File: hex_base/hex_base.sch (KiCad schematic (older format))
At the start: 41 parts, among them J1 ESP_proc, J10 PANEL5, J2 E75_proc, J3 USB_C, J4 PANEL0, J5 PANEL0, J6 PANEL1, J7 PANEL2, J8 PANEL3, J9 PANEL4, P1 TC2030-ESP, P2 TC2030-E75, U1 ESP32-WROOM-32, U2 E75-2G4M20S, U3 AMS1117-3.3

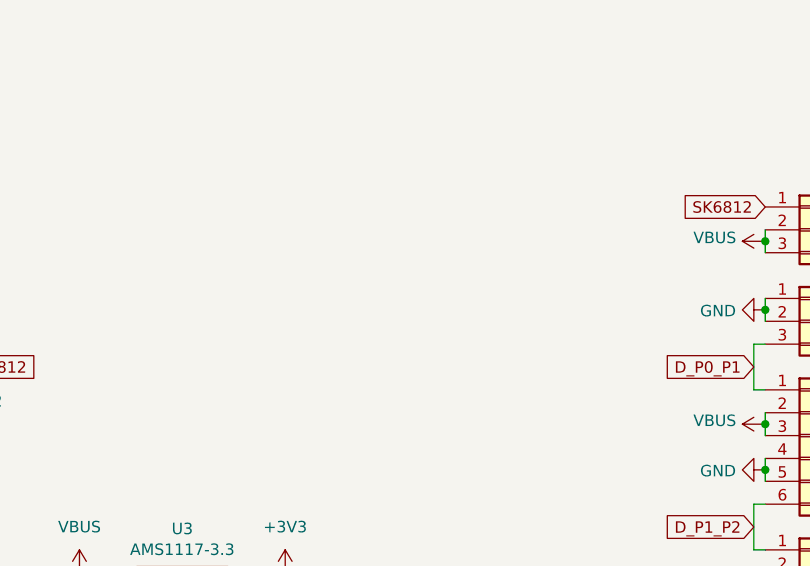
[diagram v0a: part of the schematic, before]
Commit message: fitted led board onto base, todo: buttons, fix light sensor, more caps?, silkscreen
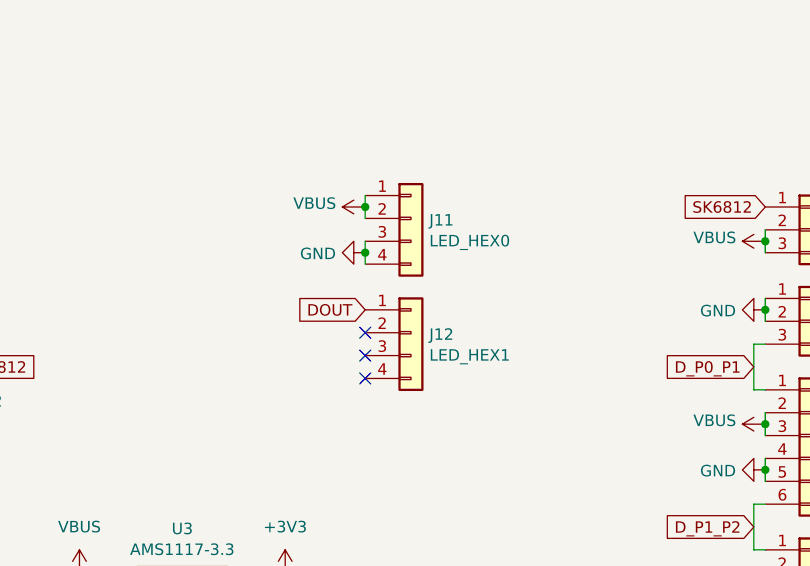
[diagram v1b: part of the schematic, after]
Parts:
- added J11: LED_HEX0, otter:PinSocket_1x04_P2.54mm_Vertical_center, symbol Connector_Generic:Conn_01x04
- added J12: LED_HEX1, otter:PinSocket_1x04_P2.54mm_Vertical_center, symbol Connector_Generic:Conn_01x04
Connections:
- net DOUT: now also J12.1 (Pin_1)
- net GND: now also J11.3 (Pin_3), J11.4 (Pin_4)
- net VBUS: now also J11.1 (Pin_1), J11.2 (Pin_2)
- no-connect marks 41 -> 44
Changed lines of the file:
@@
 Wire Wire Line
 	8300 1900 8300 1950
-Text GLabel 8300 5550 0    50   Input ~ 0
-DOUT
 Wire Wire Line
 	1800 6950 1800 7600
@@
 Wire Wire Line
 	1800 6950 2000 6950
+$Comp
+L Connector_Generic:Conn_01x04 J11
+U 1 1 61E2192F
+P 6750 1500
+F 0 "J11" H 6830 1492 50  0000 L CNN
+F 1 "LED_HEX0" H 6830 1401 50  0000 L CNN
+F 2 "otter:PinSocket_1x04_P2.54mm_Vertical_center" H 6750 1500 50  0001 C CNN
+F 3 "~" H 6750 1500 50  0001 C CNN
+	1    6750 1500
+	1    0    0    -1
+$EndComp
+Wire Wire Line
+	6550 1500 6550 1450
+Wire Wire Line
+	6550 1600 6550 1650
+Text GLabel 8300 5550 0    50   Input ~ 0
+DOUT
+Text GLabel 6550 1900 0    50   Input ~ 0
+DOUT
+$Comp
+L power:VBUS #PWR0151
+U 1 1 61E2EE7B
+P 6550 1450
+F 0 "#PWR0151" H 6550 1300 50  0001 C CNN
+F 1 "VBUS" V 6565 1577 50  0000 L CNN
+F 2 "" H 6550 1450 50  0001 C CNN
+F 3 "" H 6550 1450 50  0001 C CNN
+	1    6550 1450
+	0    -1   -1   0
+$EndComp
+$Comp
+L otter:GND #PWR0152
+U 1 1 61E2EE81
+P 6550 1650
+F 0 "#PWR0152" H 6550 1400 50  0001 C CNN
+F 1 "GND" V 6555 1522 50  0000 R CNN
+F 2 "" H 6550 1650 60  0000 C CNN
+F 3 "" H 6550 1650 60  0000 C CNN
+	1    6550 1650
+	0    1    1    0
+$EndComp
+Connection ~ 6550 1450
+Wire Wire Line
+	6550 1450 6550 1400
+Connection ~ 6550 1650
+Wire Wire Line
+	6550 1650 6550 1700
+NoConn ~ 6550 2000
+$Comp
+L Connector_Generic:Conn_01x04 J12
+U 1 1 61E22468
+P 6750 2000
+F 0 "J12" H 6830 1992 50  0000 L CNN
+F 1 "LED_HEX1" H 6830 1901 50  0000 L CNN
+F 2 "otter:PinSocket_1x04_P2.54mm_Vertical_center" H 6750 2000 50  0001 C CNN
+F 3 "~" H 6750 2000 50  0001 C CNN
+	1    6750 2000
+	1    0    0    -1
+$EndComp
+NoConn ~ 6550 2100
+NoConn ~ 6550 2200
 $EndSCHEMATC

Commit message: finished base, exported gerber
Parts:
- added C12: 100n, otter:C_0402, symbol Device:C_Small
- added R15: 100k, otter:R_0402, symbol Device:R_Small
- added SW1: RST, Button_Switch_SMD:SW_SPST_PTS810, symbol Switch:SW_Push
- added SW2: BIND, Button_Switch_SMD:SW_SPST_PTS810, symbol Switch:SW_Push
- R1: footprint otter:R_0402 -> otter:R_0805
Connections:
- net E75_RST: now also SW2.2
- net ESP_EN: now also SW1.2
- net GND: now also C12.2, SW1.1, SW2.1
- net PWM_1: now also R15.2
- net at U1.8 (IO32): now also C12.1, R15.1
- no-connect marks 44 -> 43
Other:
- moved on the sheet: J1
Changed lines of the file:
@@
 	1    0    0    -1
 $EndComp
-Text GLabel 1900 5950 0    50   Input ~ 0
+Text GLabel 1750 5850 1    50   Input ~ 0
 E75_RST
 NoConn ~ 2000 6150
@@
 $EndComp
 Wire Wire Line
-	1900 5950 1950 5950
-Wire Wire Line
 	1950 5850 1950 5950
 Connection ~ 1950 5950
@@
 NoConn ~ 3100 3250
 NoConn ~ 3100 3450
-NoConn ~ 3100 3950
 NoConn ~ 3100 3850
 NoConn ~ 3100 3750
@@
 	3100 4050 4000 4050
 $Comp
-L Device:R_Small R10
-U 1 1 61CCA13E
-P 4200 4050
-F 0 "R10" V 4500 4100 50  0000 C CNN
-F 1 "100k" V 4500 3900 50  0000 C CNN
-F 2 "otter:R_0402" H 4200 4050 50  0001 C CNN
-F 3 "~" H 4200 4050 50  0001 C CNN
-	1    4200 4050
-	0    -1   -1   0
-$EndComp
-$Comp
 L Device:R_Small R11
 U 1 1 61CCA8FD
 P 4200 4150
-F 0 "R11" V 4500 4200 50  0000 C CNN
-F 1 "100k" V 4500 4000 50  0000 C CNN
+F 0 "R11" V 4650 4200 50  0000 C CNN
+F 1 "100k" V 4650 4000 50  0000 C CNN
 F 2 "otter:R_0402" H 4200 4150 50  0001 C CNN
 F 3 "~" H 4200 4150 50  0001 C CNN
@@
 U 1 1 61CCAB94
 P 4200 4250
-F 0 "R12" V 4500 4300 50  0000 C CNN
-F 1 "100k" V 4500 4100 50  0000 C CNN
+F 0 "R12" V 4650 4300 50  0000 C CNN
+F 1 "100k" V 4650 4100 50  0000 C CNN
 F 2 "otter:R_0402" H 4200 4250 50  0001 C CNN
 F 3 "~" H 4200 4250 50  0001 C CNN
@@
 F 0 "R1" H 1020 2096 50  0000 L CNN
 F 1 "R_PHOTO" H 1020 2005 50  0000 L CNN
-F 2 "otter:R_0402" V 1000 1800 50  0001 L CNN
+F 2 "otter:R_0805" V 1000 1800 50  0001 L CNN
 F 3 "~" H 950 2000 50  0001 C CNN
 	1    950  2050
@@
 Wire Wire Line
 	1800 1850 1800 1950
-Wire Wire Line
-	1800 1950 1750 1950
 Connection ~ 1800 1950
-Text GLabel 1750 1950 0    50   Input ~ 0
+Text GLabel 1500 1600 1    50   Input ~ 0
 ESP_EN
 Text GLabel 3100 2050 2    50   Input ~ 0
@@
 L Connector_Generic:Conn_01x05 J1
 U 1 1 61CE5F79
-P 900 1100
-F 0 "J1" H 818 675 50  0000 C CNN
-F 1 "ESP_proc" H 818 766 50  0000 C CNN
-F 2 "Connector_PinHeader_2.54mm:PinHeader_1x05_P2.54mm_Vertical" H 900 1100 50  0001 C CNN
-F 3 "~" H 900 1100 50  0001 C CNN
-	1    900  1100
+P 850 4400
+F 0 "J1" H 768 3975 50  0000 C CNN
+F 1 "ESP_proc" H 768 4066 50  0000 C CNN
+F 2 "Connector_PinHeader_2.54mm:PinHeader_1x05_P2.54mm_Vertical" H 850 4400 50  0001 C CNN
+F 3 "~" H 850 4400 50  0001 C CNN
+	1    850  4400
 	-1   0    0    1
 $EndComp
@@
 L otter:GND #PWR0123
 U 1 1 61CE6E5C
-P 1100 1300
-F 0 "#PWR0123" H 1100 1050 50  0001 C CNN
-F 1 "GND" H 1105 1127 50  0000 C CNN
-F 2 "" H 1100 1300 60  0000 C CNN
-F 3 "" H 1100 1300 60  0000 C CNN
-	1    1100 1300
-	1    0    0    -1
-$EndComp
-Text GLabel 1100 1000 2    50   Input ~ 0
+P 1050 4600
+F 0 "#PWR0123" H 1050 4350 50  0001 C CNN
+F 1 "GND" H 1055 4427 50  0000 C CNN
+F 2 "" H 1050 4600 60  0000 C CNN
+F 3 "" H 1050 4600 60  0000 C CNN
+	1    1050 4600
+	1    0    0    -1
+$EndComp
+Text GLabel 1050 4300 2    50   Input ~ 0
 ESP_EN
-Text GLabel 1100 1200 2    50   Input ~ 0
+Text GLabel 1050 4500 2    50   Input ~ 0
 ESP_RX
-Text GLabel 1100 900  2    50   Input ~ 0
+Text GLabel 1050 4200 2    50   Input ~ 0
 ESP_IO0
-Text GLabel 1100 1100 2    50   Input ~ 0
+Text GLabel 1050 4400 2    50   Input ~ 0
 ESP_TX
 $Comp
@@
 NoConn ~ 6550 2100
 NoConn ~ 6550 2200
+$Comp
+L Switch:SW_Push SW2
+U 1 1 61CCEA74
+P 1450 5950
+F 0 "SW2" H 1450 6235 50  0000 C CNN
+F 1 "BIND" H 1450 6144 50  0000 C CNN
+F 2 "Button_Switch_SMD:SW_SPST_PTS810" H 1450 6150 50  0001 C CNN
+F 3 "~" H 1450 6150 50  0001 C CNN
+	1    1450 5950
+	1    0    0    -1
+$EndComp
+Wire Wire Line
+	1650 5950 1750 5950
+Wire Wire Line
+	1750 5850 1750 5950
+Connection ~ 1750 5950
+Wire Wire Line
+	1750 5950 1950 5950
+$Comp
+L otter:GND #PWR0153
+U 1 1 61CD4FA4
+P 1250 5950
+F 0 "#PWR0153" H 1250 5700 50  0001 C CNN
+F 1 "GND" V 1255 5822 50  0000 R CNN
+F 2 "" H 1250 5950 60  0000 C CNN
+F 3 "" H 1250 5950 60  0000 C CNN
+	1    1250 5950
+	0    1    1    0
+$EndComp
+$Comp
+L Switch:SW_Push SW1
+U 1 1 61CD791A
+P 1200 1600
+F 0 "SW1" H 1200 1885 50  0000 C CNN
+F 1 "RST" H 1200 1794 50  0000 C CNN
+F 2 "Button_Switch_SMD:SW_SPST_PTS810" H 1200 1800 50  0001 C CNN
+F 3 "~" H 1200 1800 50  0001 C CNN
+	1    1200 1600
+	1    0    0    -1
+$EndComp
+$Comp
+L otter:GND #PWR0154
+U 1 1 61CD7920
+P 1000 1600
+F 0 "#PWR0154" H 1000 1350 50  0001 C CNN
+F 1 "GND" V 1005 1472 50  0000 R CNN
+F 2 "" H 1000 1600 60  0000 C CNN
+F 3 "" H 1000 1600 60  0000 C CNN
+	1    1000 1600
+	0    1    1    0
+$EndComp
+Wire Wire Line
+	1500 1950 1500 1600
+Wire Wire Line
+	1500 1600 1400 1600
+Wire Wire Line
+	1500 1950 1800 1950
+Text GLabel 4300 3950 2    50   Input ~ 0
+PWM_1
+$Comp
+L Device:R_Small R10
+U 1 1 61CCA13E
+P 4200 4050
+F 0 "R10" V 4650 4100 50  0000 C CNN
+F 1 "100k" V 4650 3900 50  0000 C CNN
+F 2 "otter:R_0402" H 4200 4050 50  0001 C CNN
+F 3 "~" H 4200 4050 50  0001 C CNN
+	1    4200 4050
+	0    -1   -1   0
+$EndComp
+$Comp
+L Device:R_Small R15
+U 1 1 61CECD9B
+P 4200 3950
+F 0 "R15" V 4650 4000 50  0000 C CNN
+F 1 "100k" V 4650 3800 50  0000 C CNN
+F 2 "otter:R_0402" H 4200 3950 50  0001 C CNN
+F 3 "~" H 4200 3950 50  0001 C CNN
+	1    4200 3950
+	0    -1   -1   0
+$EndComp
+Wire Wire Line
+	4100 3950 3600 3950
+$Comp
+L Device:C_Small C12
+U 1 1 61CF26E8
+P 3600 3800
+F 0 "C12" H 3692 3846 50  0000 L CNN
+F 1 "100n" H 3692 3755 50  0000 L CNN
+F 2 "otter:C_0402" H 3600 3800 50  0001 C CNN
+F 3 "~" H 3600 3800 50  0001 C CNN
+	1    3600 3800
+	-1   0    0    1
+$EndComp
+$Comp
+L otter:GND #PWR0155
+U 1 1 61CF26EE
+P 3600 3700
+F 0 "#PWR0155" H 3600 3450 50  0001 C CNN
+F 1 "GND" H 3605 3527 50  0000 C CNN
+F 2 "" H 3600 3700 60  0000 C CNN
+F 3 "" H 3600 3700 60  0000 C CNN
+	1    3600 3700
+	-1   0    0    1
+$EndComp
+Wire Wire Line
+	3600 3900 3600 3950
+Connection ~ 3600 3950
+Wire Wire Line
+	3600 3950 3100 3950
 $EndSCHEMATC
